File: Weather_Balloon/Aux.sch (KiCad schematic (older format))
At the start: 25 parts

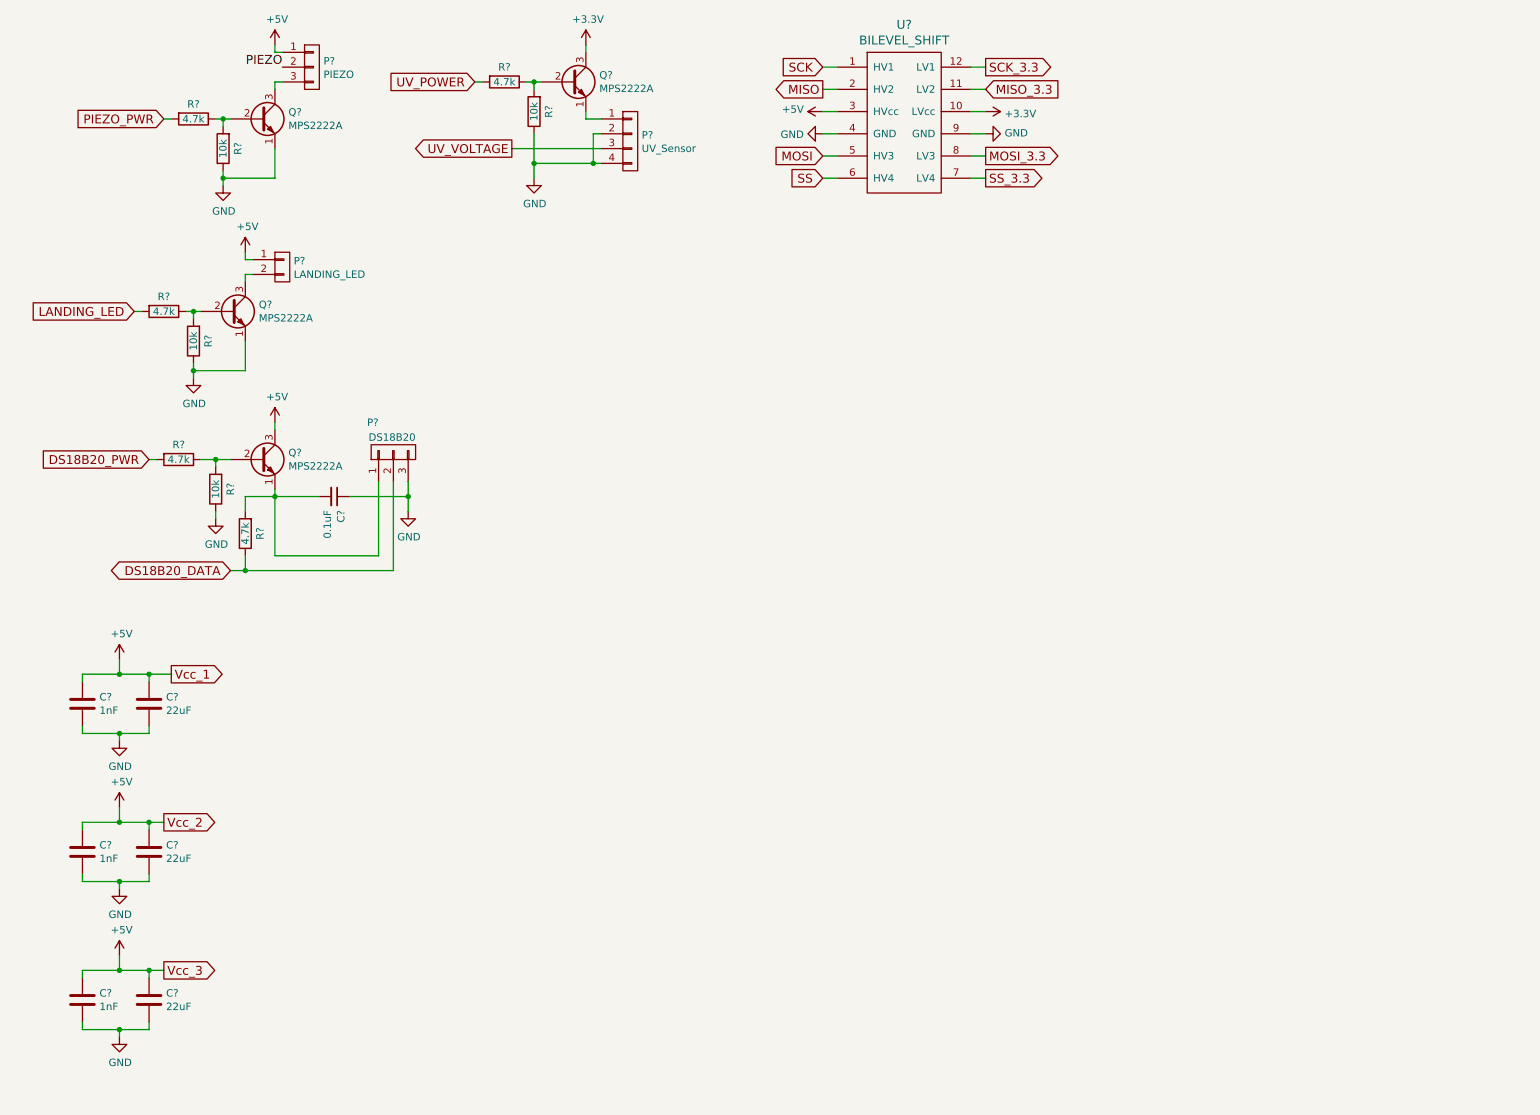
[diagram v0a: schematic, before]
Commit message: Initial PCB design with throughhole components. Layout not finilized.
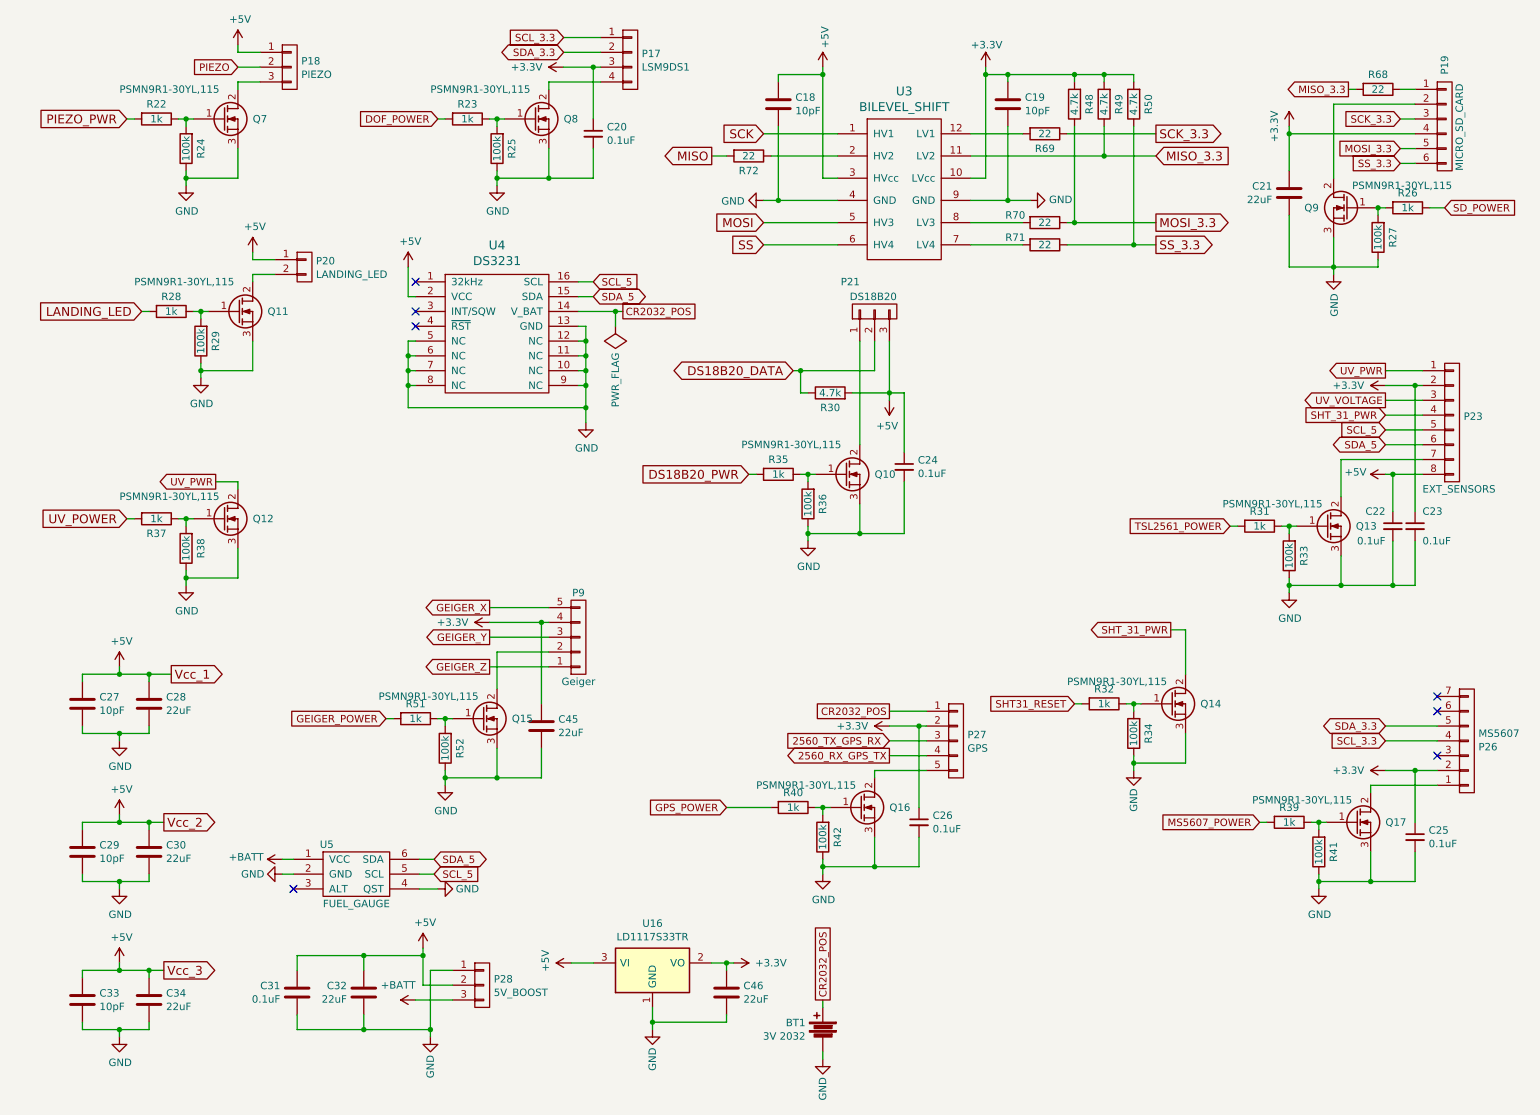
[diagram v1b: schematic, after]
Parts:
- removed P?: UV_Sensor, symbol CONN_01X04
- removed Q? (x4): MPS2222A, symbol Q_NPN_EBC
- removed R? (x3): 10k, symbol R
- removed R? (x3): 4.7k, symbol R
- added BT1: 3V 2032, Personal:CR2032, symbol Battery
- added C18, C19: 10pF, Capacitors_SMD:C_1206_HandSoldering, symbol C
- added C20, C22, C23, C25, C26: 0.1uF, Capacitors_SMD:C_1206_HandSoldering, symbol C_Small
- added C21, C32, C45, C46: 22uF, Capacitors_SMD:C_1206_HandSoldering, symbol C
- added C31: 0.1uF, Capacitors_SMD:C_1206_HandSoldering, symbol C
- added P17: LSM9DS1, Personal:LSM9DS1_BACK, symbol CONN_01X04
- added P19: MICRO_SD_CARD, Personal:MicroSD_BACK, symbol CONN_01X06
- added P23: EXT_SENSORS, Personal:Pin_Header_Straight_1x08_BACK, symbol CONN_01X08
- added P26: MS5607, Personal:MS5607_BACK, symbol CONN_01X07
- added P27: GPS, Personal:Pin_Header_Straight_1x05, symbol CONN_01X05
- added P28: 5V_BOOST, Personal:Voltage_Booster_BACK, symbol CONN_01X03
- added P9: Geiger, Personal:Pin_Header_Straight_1x05, symbol CONN_01X05
- added Q10, Q11, Q12, Q13, Q14, Q15, Q16, Q17, Q7, Q8, Q9: PSMN9R1-30YL,115, Personal:SOT-669_LFPAK, symbol Q_NMOS_GDS
- added R23, R26, R28, R31, R32, R35, R37, R39, R40, R51: 1k, Resistors_SMD:R_1206_HandSoldering, symbol R
- added R25, R27, R29, R33, R34, R36, R38, R41, R42, R52: 100k, Resistors_SMD:R_1206_HandSoldering, symbol R
- added R48, R49, R50: 4.7k, Resistors_ThroughHole:Resistor_Horizontal_RM10mm, symbol R
- added R68, R69, R70, R71, R72: 22, Resistors_ThroughHole:Resistor_Horizontal_RM10mm, symbol R
- added U16: LD1117S33TR, Power_Integrations:TO-220, symbol LD1117S33TR
- added U4: DS3231, SMD_Packages:SO-16-W, symbol DS3231
- added U5: FUEL_GAUGE, Personal:FUEL_GAUGE_BACK, symbol FUEL_GAUGE
- C24, C34: renamed from C?; footprint (none) -> Capacitors_SMD:C_1206_HandSoldering
- C27, C29, C33: renamed from C?; value 1nF -> 10pF; footprint (none) -> Capacitors_SMD:C_1206_HandSoldering
- C28, C30: renamed from C?; footprint (none) -> Capacitors_Tantalum_SMD:TantalC_SizeC_EIA-6032_HandSoldering
- P18, P21: renamed from P?; footprint (none) -> Personal:Pin_Header_Straight_1x03_BACK
- P20: renamed from P?; footprint (none) -> Personal:Pin_Header_Straight_1x02
- R22: renamed from R?; value 4.7k -> 1k; footprint (none) -> Resistors_SMD:R_1206_HandSoldering
- R24: renamed from R?; value 10k -> 100k; footprint (none) -> Resistors_SMD:R_1206_HandSoldering
- R30: renamed from R?; footprint (none) -> Resistors_ThroughHole:Resistor_Horizontal_RM10mm
- U3: renamed from U?; footprint (none) -> Personal:DIP-12_W7.62mm_LongPads_BACK
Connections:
- net +3V3: now also C19.1, C20.1, C21.1, C23.1, C25.1, C26.1, C45.2, C46.2, P17.3 (P3), P19.4 (P4), P23.2 (P2), P26.2 (P2), P27.2 (P2), P9.4 (P4), R48.2, R49.2, R50.2, U16.2 (VO)
- net +5V: now also C24.1, P21.3 (P3), R30.2, C18.1, C22.1, C31.2, C32.2, P23.8 (P8), P28.2 (P2), U16.3 (VI), U4.2 (VCC)
- net DS18B20_PWR: now also R35.2
- net GND: now also C24.2, BT1.2, C18.2, C19.2, C20.2, C21.2, C22.2, C23.2, C25.2, C26.2, C31.1, C32.1, C45.1, C46.1, P28.1 (P1), Q10.3 (S), Q11.3 (S), Q12.3 (S), Q13.3 (S), Q14.3 (S), Q15.3 (S), Q16.3 (S), Q17.3 (S), Q7.3 (S), Q8.3 (S), Q9.3 (S), R25.1, R27.1, R29.1, R33.1, R34.1, R36.1, R38.1, R41.1, R42.1, R52.1, U16.1 (GND), U4.10 (NC), U4.11 (NC), U4.12 (NC), U4.13 (GND), U4.5 (NC), U4.6 (NC), U4.7 (NC), U4.8 (NC), U4.9 (NC), U5.2 (GND), U5.4 (QST); no longer C24.1, P21.3 (P3)
- net LANDING_LED: now also R28.2
- net MISO: now also R72.2; no longer U3.2 (HV2)
- net MISO_3.3: now also R49.1, R68.2
- net MOSI_3.3: now also P19.5 (P5), R48.1, R70.1; no longer U3.8 (LV3)
- net SCK_3.3: now also P19.3 (P3), R69.1; no longer U3.12 (LV1)
- net SS_3.3: now also P19.6 (P6), R50.1, R71.1; no longer U3.7 (LV4)
- net UV_POWER: now also R37.2
- net UV_VOLTAGE: now also P23.3 (P3)
- net at R22.1, R24.2: now also Q7.1 (G)
- net at P18.3 (P3): now also Q7.2 (D)
- net at P20.2 (P2): now also Q11.2 (D)
- new net: R69.2, U3.12 (LV1)
- new net: R72.1, U3.2 (HV2)
- new net: R71.2, U3.7 (LV4)
- new net: R70.2, U3.8 (LV3)
- new net: P21.1 (P1), Q10.2 (D)
- new net: Q8.1 (G), R23.1, R25.2
- new net: P17.4 (P4), Q8.2 (D)
- new net: Q12.1 (G), R37.1, R38.2
- new net: Q15.1 (G), R51.1, R52.2
- new net: P9.2 (P2), Q15.2 (D)
- new net: Q16.1 (G), R40.1, R42.2
- new net: P27.5 (P5), Q16.2 (D)
- new net: Q14.1 (G), R32.1, R34.2
- new net: Q17.1 (G), R39.1, R41.2
- new net: P26.1 (P1), Q17.2 (D)
- new net: Q13.1 (G), R31.1, R33.2
- new net: P23.7 (P7), Q13.2 (D)
- new net: P19.1 (P1), R68.1
- new net: P19.2 (P2), Q9.2 (D)
- new net: Q9.1 (G), R26.2, R27.2
- new net: Q10.1 (G), R35.1, R36.2
- new net: Q11.1 (G), R28.1, R29.2
- new net +BATT: P28.3 (P3), U5.1 (VCC)
- new net 2560_RX_GPS_TX: P27.4 (P4)
- new net 2560_TX_GPS_RX: P27.3 (P3)
- new net CR2032_POS: BT1.1, P27.1 (P1), U4.14 (V_BAT)
- new net DOF_POWER: R23.2
- new net GEIGER_POWER: R51.2
- new net GEIGER_X: P9.5 (P5)
- new net GEIGER_Y: P9.3 (P3)
- new net GEIGER_Z: P9.1 (P1)
- new net GPS_POWER: R40.2
- new net MS5607_POWER: R39.2
- new net SCL_3.3: P17.1 (P1), P26.4 (P4)
- new net SCL_5: P23.5 (P5), U4.16 (SCL), U5.5 (SCL)
- new net SDA_3.3: P17.2 (P2), P26.5 (P5)
- new net SDA_5: P23.6 (P6), U4.15 (SDA), U5.6 (SDA)
- new net SD_POWER: R26.1
- new net SHT31_RESET: R32.2
- new net SHT_31_PWR: P23.4 (P4), Q14.2 (D)
- new net TSL2561_POWER: R31.2
- new net UV_PWR: P23.1 (P1), Q12.2 (D)
- no-connect marks 0 -> 7
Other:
- moved on the sheet: C24, P18, P20, P21, R22, R24, R30, U3

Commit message: Before manual trace width adjust
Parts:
- added P11: UV_ADC, Pin_Headers:Pin_Header_Straight_1x01, symbol CONN_01X01
- added P3: SENSOR_I2C, Pin_Headers:Pin_Header_Straight_1x04, symbol CONN_01X04
- P17: footprint Personal:LSM9DS1_BACK -> Personal:LSM9DS1_ALL
- P18, P21: footprint Personal:Pin_Header_Straight_1x03_BACK -> Pin_Headers:Pin_Header_Straight_1x03
- P19: footprint Personal:MicroSD_BACK -> Personal:MicroSD_ALL
- P20: footprint Personal:Pin_Header_Straight_1x02 -> Pin_Headers:Pin_Header_Straight_1x02
- P23: footprint Personal:Pin_Header_Straight_1x08_BACK -> Pin_Headers:Pin_Header_Straight_1x05; symbol CONN_01X08 -> CONN_01X05
- P26: footprint Personal:MS5607_BACK -> Personal:MS5607_ALL
- P27, P9: footprint Personal:Pin_Header_Straight_1x05 -> Pin_Headers:Pin_Header_Straight_1x05
- P28: footprint Personal:Voltage_Booster_BACK -> Personal:Voltage_Booster_ALL
- R30, R48, R49, R50, R68, R69, R70, R71, R72: footprint Resistors_ThroughHole:Resistor_Horizontal_RM10mm -> Resistors_SMD:R_1206_HandSoldering
- U3: footprint Personal:DIP-12_W7.62mm_LongPads_BACK -> Personal:DIP-12_W7.62mm_LongPads_ALL
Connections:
- net +3V3: now also P3.1 (P1); no longer C23.1, P23.2 (P2)
- net +5V: now also P3.3 (P3); no longer C22.1, P23.8 (P8)
- net GEIGER_X: now also P9.1 (P1); no longer P9.5 (P5)
- net GEIGER_Z: now also P9.5 (P5); no longer P9.1 (P1)
- net SCL_5: now also P3.4 (P4); no longer P23.5 (P5)
- net SDA_5: now also P3.2 (P2); no longer P23.6 (P6)
- net SHT_31_PWR: now also P23.3 (P3); no longer P23.4 (P4)
- net UV_VOLTAGE: now also P11.1 (P1); no longer P23.3 (P3)
- net at Q13.2 (D): now also P23.4 (P4); no longer P23.7 (P7)
- new net: C23.1, P23.2 (P2)
- new net: C22.1, P23.5 (P5)
